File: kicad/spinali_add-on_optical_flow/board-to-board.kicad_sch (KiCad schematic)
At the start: 6 parts, among them J1 DF40TC(4.0)-50DS-0.4V(51), J2 DF40TC(4.0)-50DS-0.4V(51)

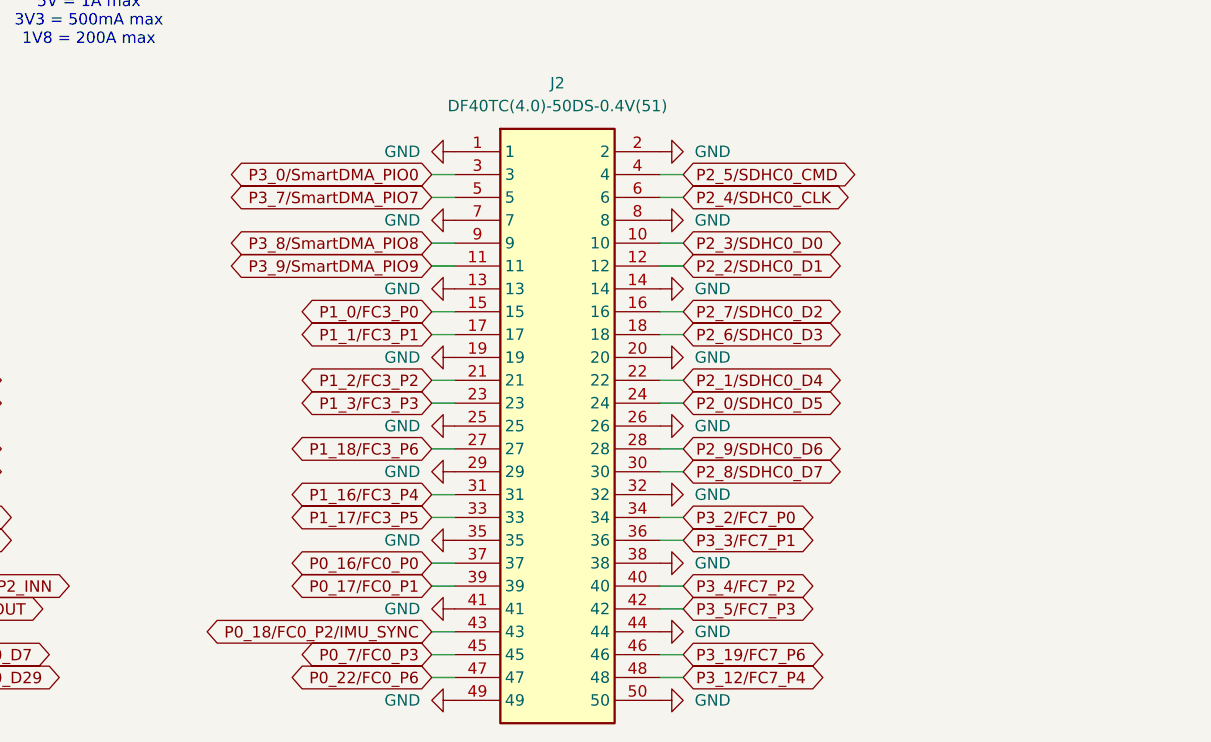
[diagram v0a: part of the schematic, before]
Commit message: Updated schematic and started on layout
- Added LED driver circuit for PAA3905 LED_SYNC.
- Started on layouting PCB.
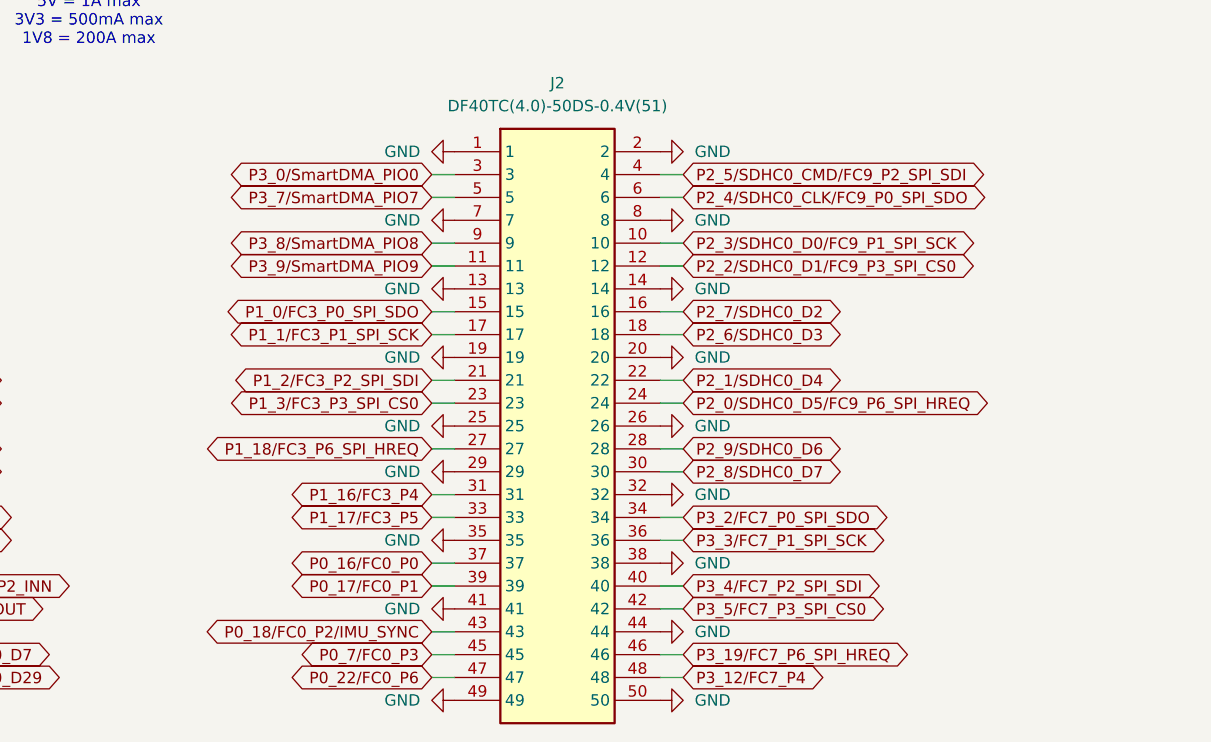
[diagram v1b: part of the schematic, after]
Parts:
- J1, J2: DigiKey (none) -> 26-DF40TC(4.0)-50DS-0.4V(51)CT-ND; MF (none) -> Hirose; MFPN (none) -> DF40TC(4.0)-50DS-0.4V(51)
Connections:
- net P1_0/FC3_P0 renamed P1_0/FC3_P0_SPI_SDO
- net P1_18/FC3_P6 renamed P1_18/FC3_P6_SPI_HREQ
- net P1_1/FC3_P1 renamed P1_1/FC3_P1_SPI_SCK
- net P1_2/FC3_P2 renamed P1_2/FC3_P2_SPI_SDI
- net P1_3/FC3_P3 renamed P1_3/FC3_P3_SPI_CS0
- net P2_0/SDHC0_D5 renamed P2_0/SDHC0_D5/FC9_P6_SPI_HREQ
- net P2_2/SDHC0_D1 renamed P2_2/SDHC0_D1/FC9_P3_SPI_CS0
- net P2_3/SDHC0_D0 renamed P2_3/SDHC0_D0/FC9_P1_SPI_SCK
- net P2_4/SDHC0_CLK renamed P2_4/SDHC0_CLK/FC9_P0_SPI_SDO
- net P2_5/SDHC0_CMD renamed P2_5/SDHC0_CMD/FC9_P2_SPI_SDI
- net P3_19/FC7_P6 renamed P3_19/FC7_P6_SPI_HREQ
- net P3_2/FC7_P0 renamed P3_2/FC7_P0_SPI_SDO
- net P3_3/FC7_P1 renamed P3_3/FC7_P1_SPI_SCK
- net P3_4/FC7_P2 renamed P3_4/FC7_P2_SPI_SDI
- net P3_5/FC7_P3 renamed P3_5/FC7_P3_SPI_CS0
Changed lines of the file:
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@@
 (kicad_sch
-	(version 20231120)
+	(version 20250114)
 	(generator "eeschema")
-	(generator_version "8.0")
+	(generator_version "9.0")
 	(paper "A4")
 	(title_block
@@
 		(comment 4 "CTO SYSTEM INNOVATIONS / MOBILE ROBOTICS DOMAIN")
 	)
+	(text "300mA max per pin\n5V = 1A max\n3V3 = 500mA max\n1V8 = 200A max"
+		(exclude_from_sim no)
+		(at 142.24 51.816 0)
+		(effects
+			(font
+				(size 1.27 1.27)
+			)
+		)
+	)
 	(junction
 		(at 116.84 82.55)
@@
 		)
 	)
-	(text "300mA max per pin\n5V = 1A max\n3V3 = 500mA max\n1V8 = 200A max"
-		(exclude_from_sim no)
-		(at 142.24 51.816 0)
-		(effects
-			(font
-				(size 1.27 1.27)
-			)
-		)
-	)
 	(global_label "P3_10{slash}FC6_P2"
 		(shape bidirectional)
@@
 		)
 	)
-	(global_label "P2_5{slash}SDHC0_CMD"
+	(global_label "P2_5/SDHC0_CMD/FC9_P2_SPI_SDI"
 		(shape bidirectional)
 		(at 208.28 69.85 0)
@@
 		)
 	)
-	(global_label "P3_2{slash}FC7_P0"
+	(global_label "P3_2{slash}FC7_P0_SPI_SDO"
 		(shape bidirectional)
 		(at 208.28 107.95 0)
@@
 		)
 		(property "Intersheetrefs" "${INTERSHEET_REFS}"
-			(at 225.3788 107.95 0)
+			(at 234.2083 107.95 0)
 			(effects
 				(font
@@
 		)
 	)
-	(global_label "P1_3{slash}FC3_P3"
+	(global_label "P1_3{slash}FC3_P3_SPI_CS0"
 		(shape bidirectional)
 		(at 180.34 95.25 180)
@@
 		)
 		(property "Intersheetrefs" "${INTERSHEET_REFS}"
-			(at 163.2412 95.25 0)
+			(at 154.5327 95.25 0)
 			(effects
 				(font
@@
 		)
 	)
-	(global_label "P2_2{slash}SDHC0_D1"
+	(global_label "P2_2/SDHC0_D1/FC9_P3_SPI_CS0"
 		(shape bidirectional)
 		(at 208.28 80.01 0)
@@
 		)
 	)
-	(global_label "P1_1{slash}FC3_P1"
+	(global_label "P1_1{slash}FC3_P1_SPI_SCK"
 		(shape bidirectional)
 		(at 180.34 87.63 180)
@@
 		)
 		(property "Intersheetrefs" "${INTERSHEET_REFS}"
-			(at 163.2412 87.63 0)
+			(at 154.4722 87.63 0)
 			(effects
 				(font
@@
 		)
 	)
-	(global_label "P1_2{slash}FC3_P2"
+	(global_label "P1_2{slash}FC3_P2_SPI_SDI"
 		(shape bidirectional)
 		(at 180.34 92.71 180)
@@
 		)
 		(property "Intersheetrefs" "${INTERSHEET_REFS}"
-			(at 163.2412 92.71 0)
+			(at 155.1374 92.71 0)
 			(effects
 				(font
@@
 		)
 	)
-	(global_label "P3_3{slash}FC7_P1"
+	(global_label "P3_3{slash}FC7_P1_SPI_SCK"
 		(shape bidirectional)
 		(at 208.28 110.49 0)
@@
 		)
 		(property "Intersheetrefs" "${INTERSHEET_REFS}"
-			(at 225.3788 110.49 0)
+			(at 234.1478 110.49 0)
 			(effects
 				(font
@@
 		)
 	)
-	(global_label "P3_5{slash}FC7_P3"
+	(global_label "P3_5{slash}FC7_P3_SPI_CS0"
 		(shape bidirectional)
 		(at 208.28 118.11 0)
@@
 		)
 		(property "Intersheetrefs" "${INTERSHEET_REFS}"
-			(at 225.3788 118.11 0)
+			(at 234.0873 118.11 0)
 			(effects
 				(font
@@
 		)
 	)
-	(global_label "P2_3{slash}SDHC0_D0"
+	(global_label "P2_3/SDHC0_D0/FC9_P1_SPI_SCK"
 		(shape bidirectional)
 		(at 208.28 77.47 0)
@@
 		)
 	)
-	(global_label "P1_0{slash}FC3_P0"
+	(global_label "P1_0{slash}FC3_P0_SPI_SDO"
 		(shape bidirectional)
 		(at 180.34 85.09 180)
@@
 		)
 		(property "Intersheetrefs" "${INTERSHEET_REFS}"
-			(at 163.2412 85.09 0)
+			(at 154.4117 85.09 0)
 			(effects
 				(font
@@
 		)
 	)
-	(global_label "P3_19{slash}FC7_P6"
+	(global_label "P3_19{slash}FC7_P6_SPI_HREQ"
 		(shape bidirectional)
 		(at 208.28 123.19 0)
@@
 		)
 		(property "Intersheetrefs" "${INTERSHEET_REFS}"
-			(at 226.5883 123.19 0)
+			(at 236.6878 123.19 0)
 			(effects
 				(font
@@
 		)
 	)
-	(global_label "P3_4{slash}FC7_P2"
+	(global_label "P3_4{slash}FC7_P2_SPI_SDI"
 		(shape bidirectional)
 		(at 208.28 115.57 0)
@@
 		)
 		(property "Intersheetrefs" "${INTERSHEET_REFS}"
-			(at 225.3788 115.57 0)
+			(at 233.4826 115.57 0)
 			(effects
 				(font
@@
 		)
 	)
-	(global_label "P1_18{slash}FC3_P6"
+	(global_label "P1_18{slash}FC3_P6_SPI_HREQ"
 		(shape bidirectional)
 		(at 180.34 100.33 180)
@@
 		)
 		(property "Intersheetrefs" "${INTERSHEET_REFS}"
-			(at 162.0317 100.33 0)
+			(at 151.9322 100.33 0)
 			(effects
 				(font
@@
 		)
 	)
-	(global_label "P2_0{slash}SDHC0_D5"
+	(global_label "P2_0/SDHC0_D5/FC9_P6_SPI_HREQ"
 		(shape bidirectional)
 		(at 208.28 95.25 0)
@@
 		)
 	)
-	(global_label "P2_4{slash}SDHC0_CLK"
+	(global_label "P2_4/SDHC0_CLK/FC9_P0_SPI_SDO"
 		(shape bidirectional)
 		(at 208.28 72.39 0)
@@
 			)
 		)
-		(property "MF" ""
-			(at 182.88 67.31 0)
-			(effects
-				(font
-					(size 1.27 1.27)
-				)
-				(hide yes)
-			)
-		)
-		(property "MFPN" ""
+		(property "MF" "Hirose"
 			(at 182.88 67.31 0)
 			(effects
@@
 			)
 		)
-		(property "Supplier" ""
+		(property "MFPN" "DF40TC(4.0)-50DS-0.4V(51)"
 			(at 182.88 67.31 0)
 			(effects
@@
 			)
 		)
-		(property "Supplier PN" ""
+		(property "DigiKey" "26-DF40TC(4.0)-50DS-0.4V(51)CT-ND"
 			(at 182.88 67.31 0)
 			(effects
@@
 			)
 		)
-		(property "MF" ""
-			(at 92.71 67.31 0)
-			(effects
-				(font
-					(size 1.27 1.27)
-				)
-				(hide yes)
-			)
-		)
-		(property "MFPN" ""
+		(property "MF" "Hirose"
 			(at 92.71 67.31 0)
 			(effects
@@
 			)
 		)
-		(property "Supplier" ""
+		(property "MFPN" "DF40TC(4.0)-50DS-0.4V(51)"
 			(at 92.71 67.31 0)
 			(effects
@@
 			)
 		)
-		(property "Supplier PN" ""
+		(property "DigiKey" "26-DF40TC(4.0)-50DS-0.4V(51)CT-ND"
 			(at 92.71 67.31 0)
 			(effects

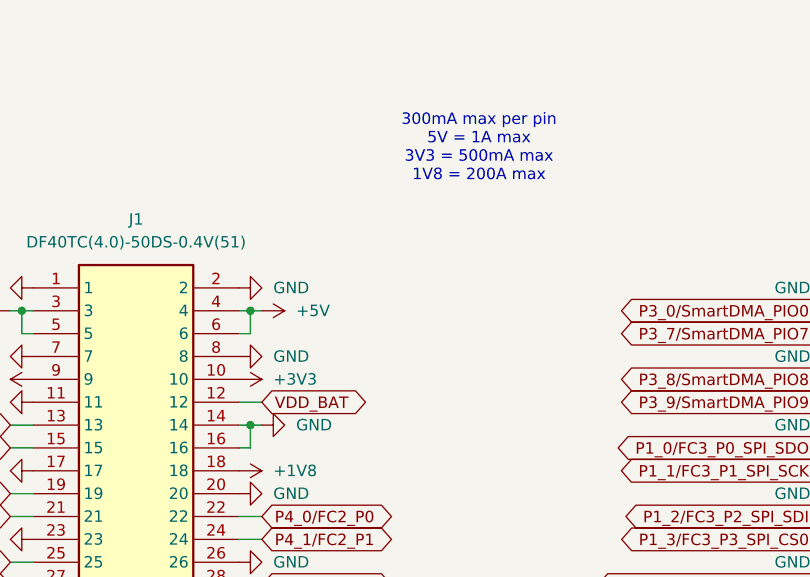
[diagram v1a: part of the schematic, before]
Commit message: Finished layout and schematic
- Added cognipilot logo to silkscreen.
- Added test points to PAA3905E1 data signals.
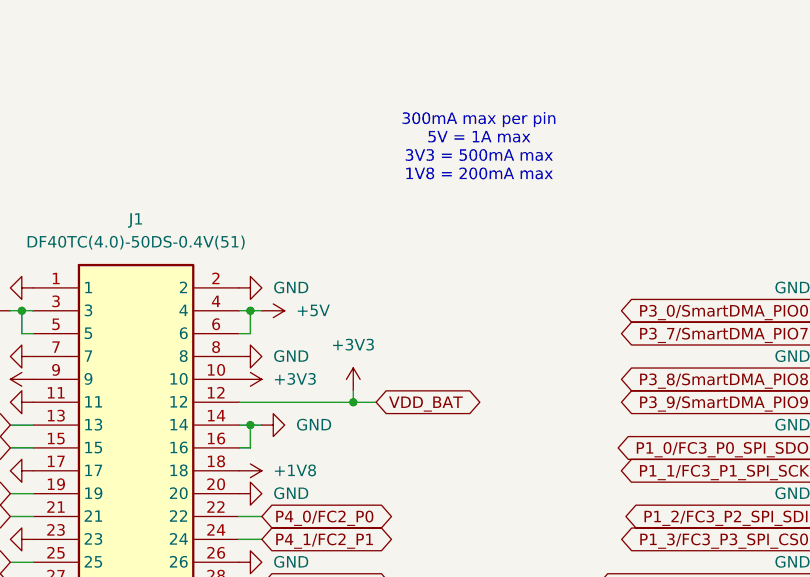
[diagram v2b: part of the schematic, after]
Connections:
- net VDD_BAT is gone; now on net +3V3: J1.12
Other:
- note added: "300mA max per pin 5V = 1A max 3V3 = 500mA max 1V8 = 200mA max"
- note removed: "300mA max per pin 5V = 1A max 3V3 = 500mA max 1V8 = 200A max"
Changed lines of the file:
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@@
 		(comment 4 "CTO SYSTEM INNOVATIONS / MOBILE ROBOTICS DOMAIN")
 	)
-	(text "300mA max per pin\n5V = 1A max\n3V3 = 500mA max\n1V8 = 200A max"
+	(text "300mA max per pin\n5V = 1A max\n3V3 = 500mA max\n1V8 = 200mA max"
 		(exclude_from_sim no)
 		(at 142.24 51.816 0)
@@
 	)
 	(junction
+		(at 128.27 80.01)
+		(diameter 0)
+		(color 0 0 0 0)
+	)
+	(junction
 		(at 91.44 69.85)
 		(diameter 0)
@@
 	(wire
 		(pts
-			(xy 118.11 80.01) (xy 115.57 80.01)
+			(xy 130.81 80.01) (xy 128.27 80.01)
 		)
 		(stroke
@@
 	(wire
 		(pts
+			(xy 128.27 78.74) (xy 128.27 80.01)
+		)
+		(stroke
+			(width 0)
+			(type default)
+		)
+	)
+	(wire
+		(pts
 			(xy 118.11 100.33) (xy 115.57 100.33)
 		)
@@
 	(wire
 		(pts
+			(xy 128.27 80.01) (xy 115.57 80.01)
+		)
+		(stroke
+			(width 0)
+			(type default)
+		)
+	)
+	(wire
+		(pts
 			(xy 208.28 123.19) (xy 205.74 123.19)
 		)
@@
 	(global_label "VDD_BAT"
 		(shape bidirectional)
-		(at 118.11 80.01 0)
-		(fields_autoplaced yes)
-		(effects
-			(font
-				(size 1.27 1.27)
-			)
-			(justify left)
-		)
-		(property "Intersheetrefs" "${INTERSHEET_REFS}"
-			(at 130.1289 80.01 0)
+		(at 130.81 80.01 0)
+		(fields_autoplaced yes)
+		(effects
+			(font
+				(size 1.27 1.27)
+			)
+			(justify left)
+		)
+		(property "Intersheetrefs" "${INTERSHEET_REFS}"
+			(at 142.8289 80.01 0)
 			(effects
 				(font
@@
 					(unit 1)
 				)
+			)
+		)
+	)
+	(symbol
+		(lib_id "power:+3V3")
+		(at 128.27 78.74 0)
+		(mirror y)
+		(unit 1)
+		(exclude_from_sim no)
+		(in_bom yes)
+		(on_board yes)
+		(dnp no)
+		(fields_autoplaced yes)
+		(property "Reference" "#PWR073"
+			(at 128.27 82.55 0)
+			(effects
+				(font
+					(size 1.27 1.27)
+				)
+				(hide yes)
+			)
+		)
+		(property "Value" "+3V3"
+			(at 128.27 73.66 0)
+			(effects
+				(font
+					(size 1.27 1.27)
+				)
+			)
+		)
+		(property "Footprint" ""
+			(at 128.27 78.74 0)
+			(effects
+				(font
+					(size 1.27 1.27)
+				)
+				(hide yes)
+			)
+		)
+		(property "Datasheet" ""
+			(at 128.27 78.74 0)
+			(effects
+				(font
+					(size 1.27 1.27)
+				)
+				(hide yes)
+			)
+		)
+		(property "Description" "Power symbol creates a global label with name \"+3V3\""
+			(at 128.27 78.74 0)
+			(effects
+				(font
+					(size 1.27 1.27)
+				)
+				(hide yes)
+			)
+		)
+		(pin "1"
+		)
+		(instances
+			(project "spinali_add-on_optical_flow"
+				(path "/04285d74-eeba-483c-9378-52bd287e15a2/ccc0d483-c16f-4a48-802e-c15323fec247"
+					(reference "#PWR073")
+					(unit 1)
+				)
